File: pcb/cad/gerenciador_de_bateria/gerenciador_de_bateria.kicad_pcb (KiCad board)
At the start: 2 copper layers, 41.1 x 24.9 mm, 31 parts, among them J1 Conn_01x02_Male, J14 Conn_01x03_Male, J2 Conn_01x03_Male, J3 Conn_01x02_Male, SW1 SW_Push, U1 USB_BQ25629, U2 BQ25629

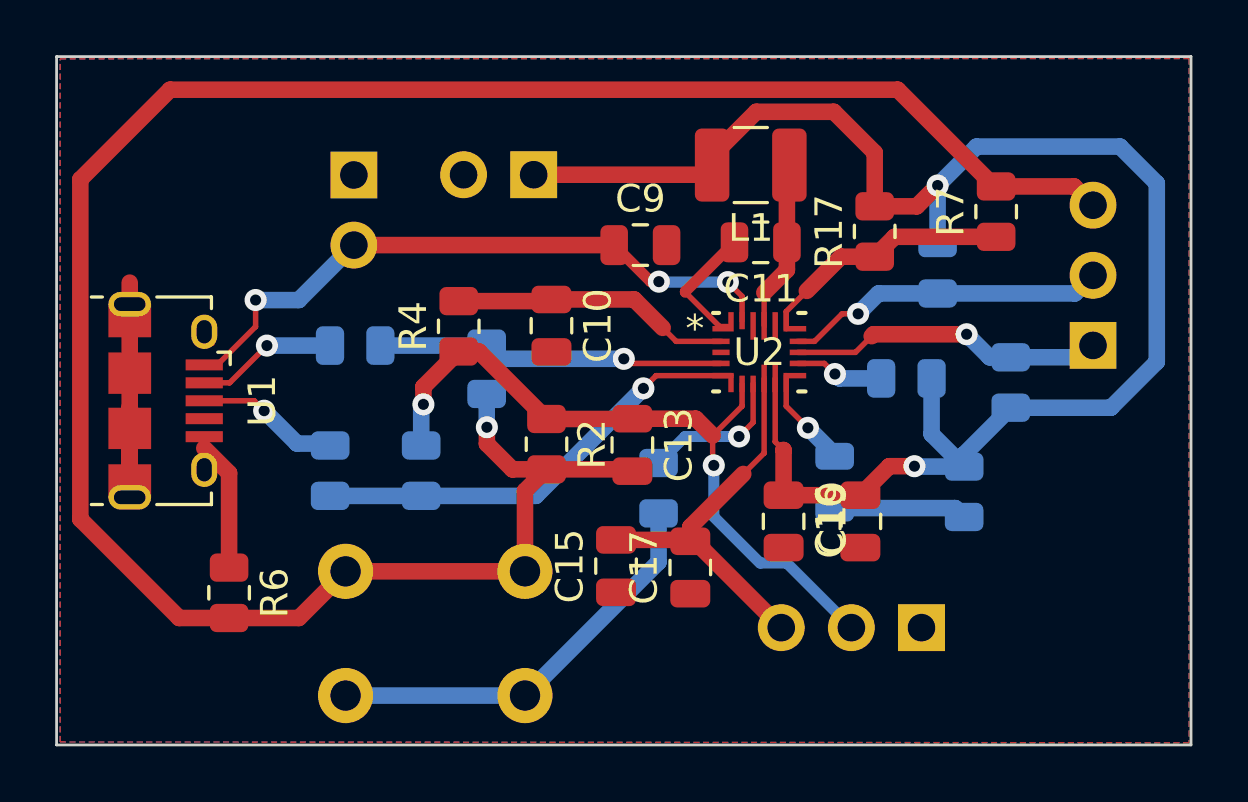
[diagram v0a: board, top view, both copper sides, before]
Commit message: Otimização e diminuição da PCB do gerenciador_de_bateria
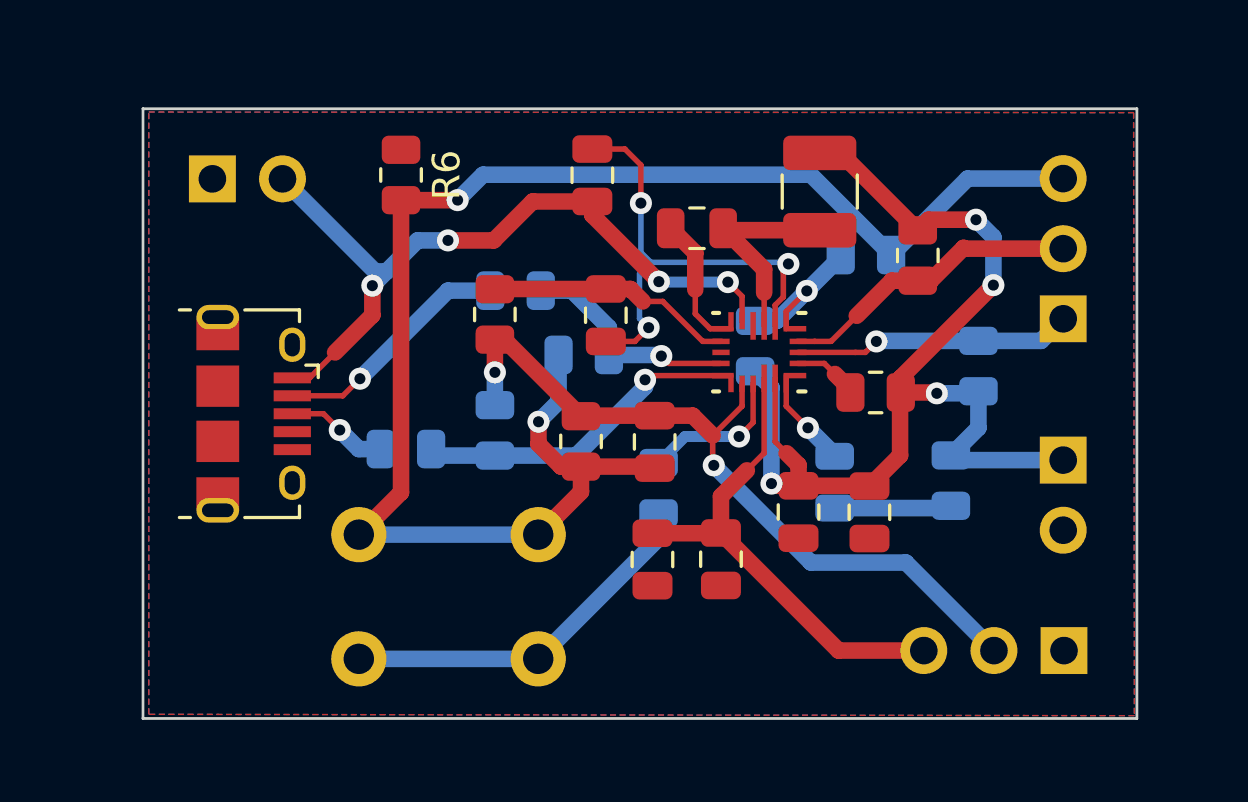
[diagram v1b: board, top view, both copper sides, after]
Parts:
- R13, R16: moved to F.Cu
- R17, R7: moved to B.Cu
- moved J1 21.8 mm to (172.6, 109.2), turned to 180 degrees
- moved R6 16.4 mm to (148.6, 98.9)
- moved R3 6.14 mm to (152.8, 103.0)
- moved R17 6.00 mm to (161.5, 105.1), turned to -90 degrees
- moved J2 5.23 mm to (172.7, 116.1)
- moved J3 5.13 mm to (141.8, 99.0), turned to -90 degrees
- moved R7 4.97 mm to (165.5, 101.8), turned to 0 degrees
- moved R24 3.55 mm to (155.3, 105.4), turned to 180 degrees
- moved U1 3.22 mm to (143.3, 107.5)
- moved C9 3.07 mm to (155.6, 98.9), turned to 90 degrees
- moved R1 3.04 mm to (152.0, 108.1)
- moved R5 2.86 mm to (148.8, 108.8), turned to 0 degrees
- moved L1 2.68 mm to (163.8, 99.5), turned to 90 degrees
- moved C11 2.37 mm to (159.4, 100.8)
- moved C10 2.01 mm to (156.1, 103.9)
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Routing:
- net GNDA: track 81.9 -> 57.2 mm, vias 1 -> 2
- net /SYS: track 60.1 -> 40.6 mm, vias 2 -> 4
- net /D-_ILIM: track 12.7 -> 8.17 mm
- net /D+_TSBIAS: track 16.3 -> 12.3 mm
- net /VIN: track 23.5 -> 27.3 mm, vias 3 -> 4
- net Net-(R3-Pad1): track 5.11 -> 8.76 mm
- net //CE: track 9.35 -> 5.81 mm, vias 0 -> 1
- net /BAT: track 14.3 -> 17.8 mm
- net GNDPWR: track 14.5 -> 17.6 mm, vias 0 -> 3
- net /TS: track 26.4 -> 28.1 mm
- net Net-(R10-Pad2): track 15.1 -> 13.6 mm
- net Net-(R5-Pad1): track 5.23 -> 3.74 mm
- net /SW: track 6.31 -> 7.68 mm
- net /SDA: track 11.5 -> 10.2 mm
- net /REGN: track 10.2 -> 8.98 mm
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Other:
- board size 41.1 x 24.9 mm -> 36 x 22.1 mm

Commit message: Alteração dos conectores no esquemático para o rearranjo e a diminuição da PCB que foi feita no gerenciador_de_bateria
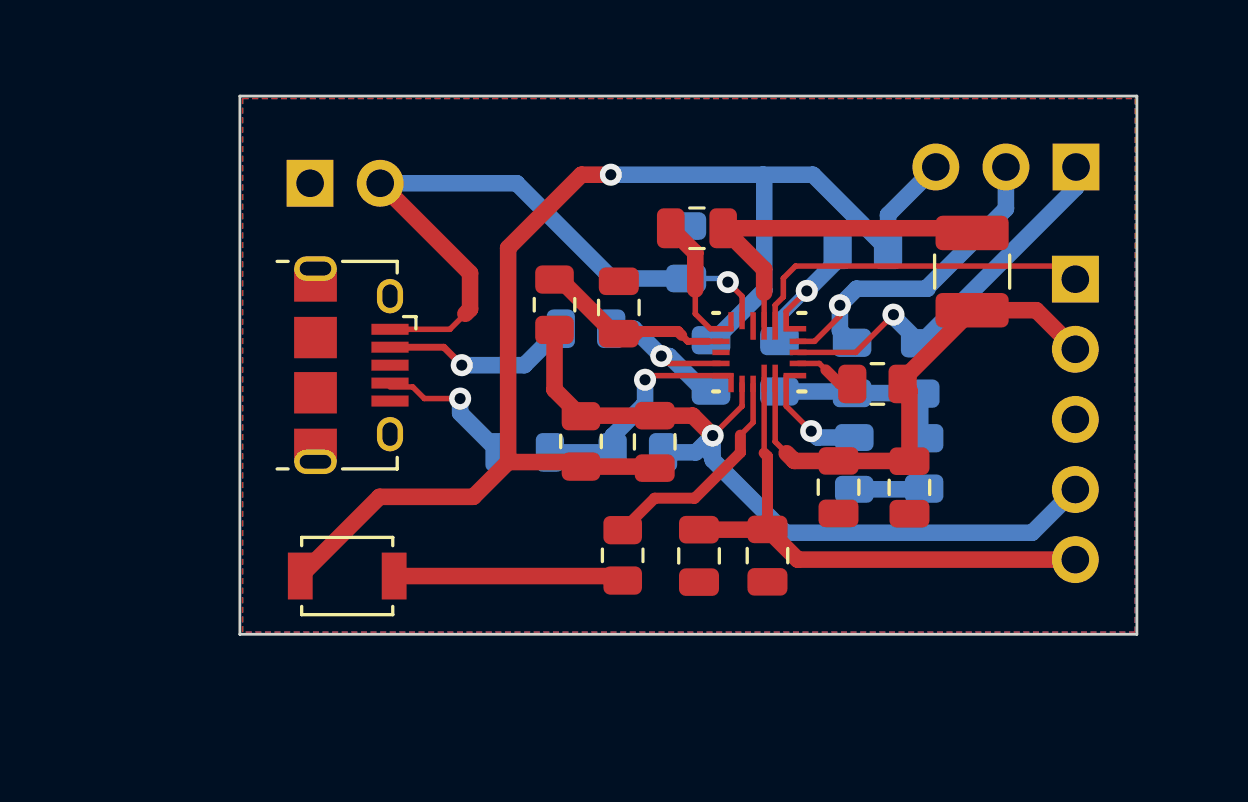
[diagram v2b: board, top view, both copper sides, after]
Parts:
- removed J1: Conn_01x02_Male, Connector_PinHeader_2.54mm:PinHeader_1x02_P2.54mm_Vertical
- removed J2: Conn_01x03_Male, Connector_PinHeader_2.54mm:PinHeader_1x03_P2.54mm_Vertical
- removed R6: 0, Resistor_SMD:R_0805_2012Metric
- added J4: Conn_01x05_Male, Connector_PinHeader_2.54mm:PinHeader_1x05_P2.54mm_Vertical, B.Cu at (173.1, 102.6)
- C9, R13: moved to B.Cu
- R10: moved to F.Cu
- SW1: footprint Button_Switch_THT:SW_PUSH_6mm -> Button_Switch_SMD:SW_SPST_B3U-1000P; moved to F.Cu
- moved L1 6.24 mm to (169.3, 102.4), turned to -90 degrees
- moved J14 5.52 mm to (173.1, 98.6), turned to 90 degrees
- moved R1 5.24 mm to (157.2, 108.9), turned to 0 degrees
- moved R13 4.72 mm to (165.0, 105.8), turned to -90 degrees
- moved R24 4.63 mm to (159.9, 105.8), turned to 90 degrees
- moved C9 4.40 mm to (159.0, 101.7)
- moved R5 4.30 mm to (153.1, 108.9)
- moved U1 3.95 mm to (146.8, 105.8)
- moved J3 3.54 mm to (145.3, 99.2)
- moved SW1 3.03 mm to (146.7, 113.4), turned to 180 degrees
- moved R3 2.90 mm to (155.3, 104.4)
- moved R10 2.76 mm to (156.7, 112.6)
- moved R4 2.19 mm to (154.2, 103.6)
- moved R15 2.11 mm to (167.4, 105.9)
- moved C16 1.71 mm to (164.5, 110.2)
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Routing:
- net /SYS: track 40.6 -> 25.2 mm, vias 4 -> 0
- net GNDA: track 57.2 -> 49.0 mm, vias 2 -> 1
- net /SW: track 7.68 -> 13.2 mm
- net Net-(R10-Pad2): track 13.6 -> 8.35 mm
- net GNDPWR: track 17.6 -> 12.8 mm, vias 3 -> 0
- net /SDA: track 10.2 -> 14.2 mm
- net /D+_TSBIAS: track 12.3 -> 8.57 mm
- net //QON: track 5.43 -> 8.18 mm, vias 1 -> 0
- net /VIN: track 27.3 -> 24.8 mm, vias 4 -> 1
- net /REGN: track 8.98 -> 6.74 mm
- net /SCL: track 11.0 -> 12.8 mm, vias 0 -> 1
- net /BAT: track 17.8 -> 19.7 mm
- net Net-(D6-Pad2): track 4.24 -> 2.54 mm
- net Net-(R3-Pad1): track 8.76 -> 7.20 mm
- net Net-(R5-Pad1): track 3.74 -> 5.26 mm
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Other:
- board size 36 x 22.1 mm -> 32.5 x 19.5 mm
